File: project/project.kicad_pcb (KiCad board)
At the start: 4 copper layers, 84 x 41 mm, 86 parts, among them J101 BUS, J102 BUS, J103 Back, J201 24V, J202 3V3, J203 6V, J301 USB_C_Receptacle_USB2.0, SW301 15mm, SW302 15mm, U101 TMP102, U201 MT3406, U202 ME3121AM6G, U301 USBLC6-2SC6, U302 esp32-C3FH4X, U303 XL1050, Y301 40MHz

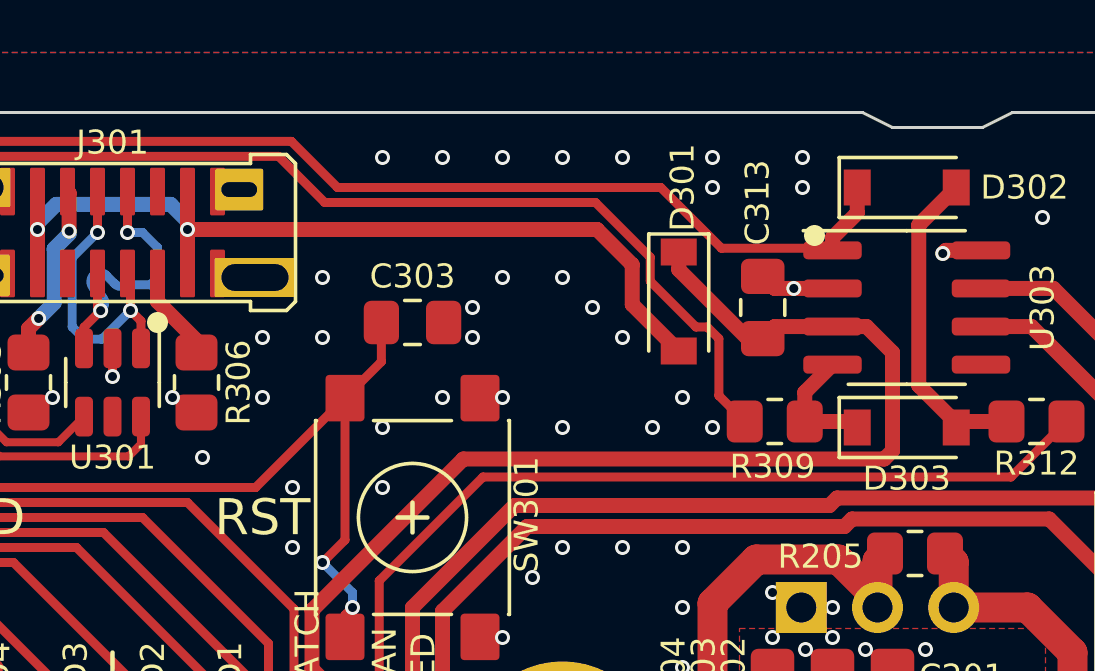
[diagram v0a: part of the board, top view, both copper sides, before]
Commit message: fixing CAN level shifting resistors
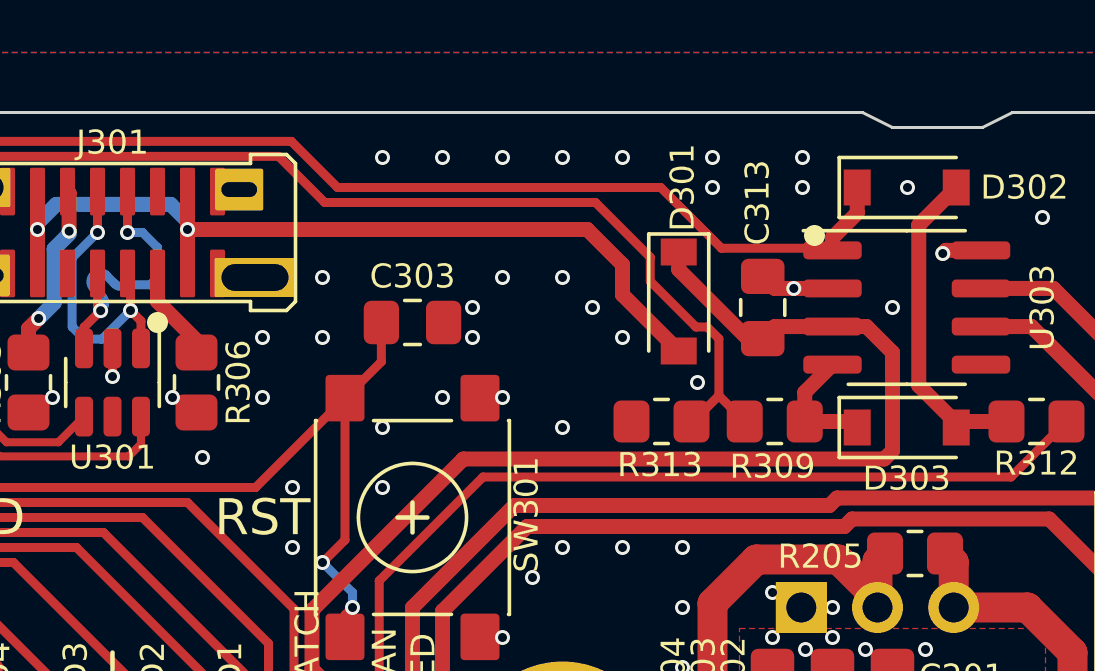
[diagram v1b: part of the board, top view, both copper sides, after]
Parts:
- removed kibuzzard-69BC7741: G***, kibuzzard-69BC7741
- added R313: 3k, Resistor_SMD:R_0805_2012Metric_Pad1.20x1.40mm_HandSolder, F.Cu at (186.6, 123.8)
- added kibuzzard-6A7A000F: G***, kibuzzard-6A7A000F, B.Cu at (189.3, 152.5)
- R309: value 4k7 -> 1k5
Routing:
- net /uC/RX: track 54.1 -> 55.3 mm
